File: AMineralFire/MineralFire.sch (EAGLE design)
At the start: 61 parts, among them IC1 LM358, Q1 20MHz, Q2 20MHz, T1 200mA/40V, U1 328P, U2 328P, U3 7805

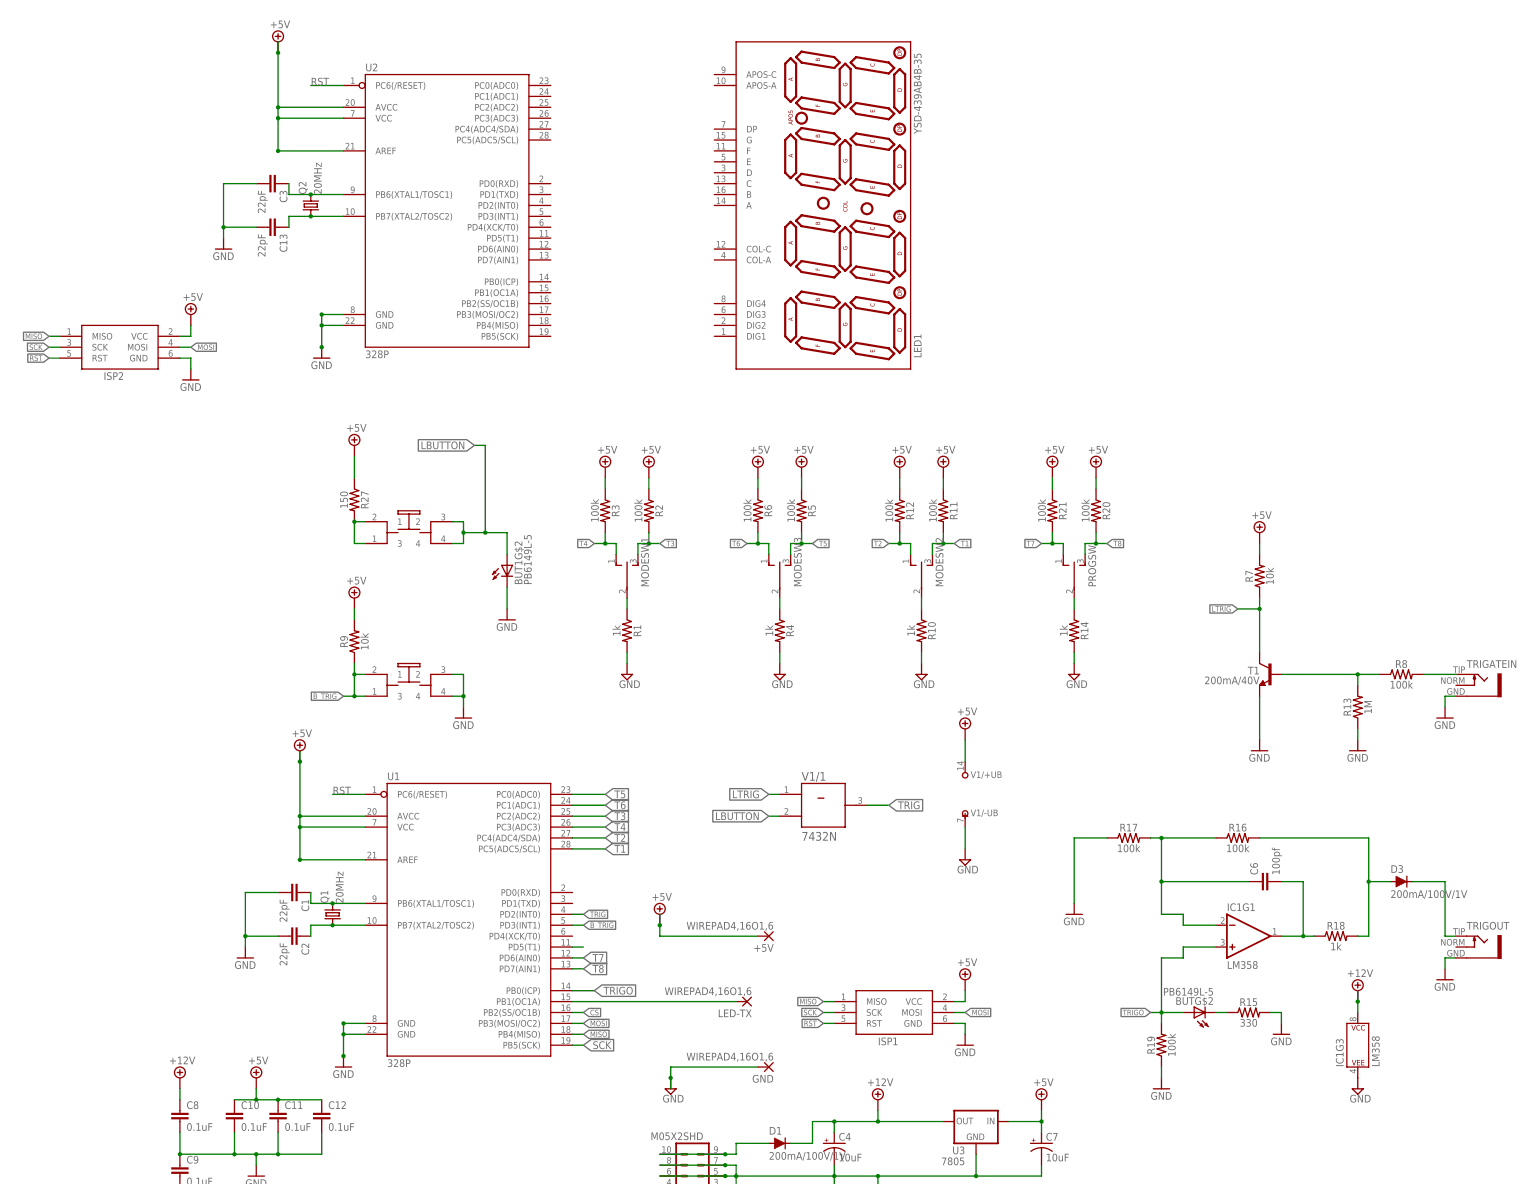
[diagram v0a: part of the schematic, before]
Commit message: adding Display
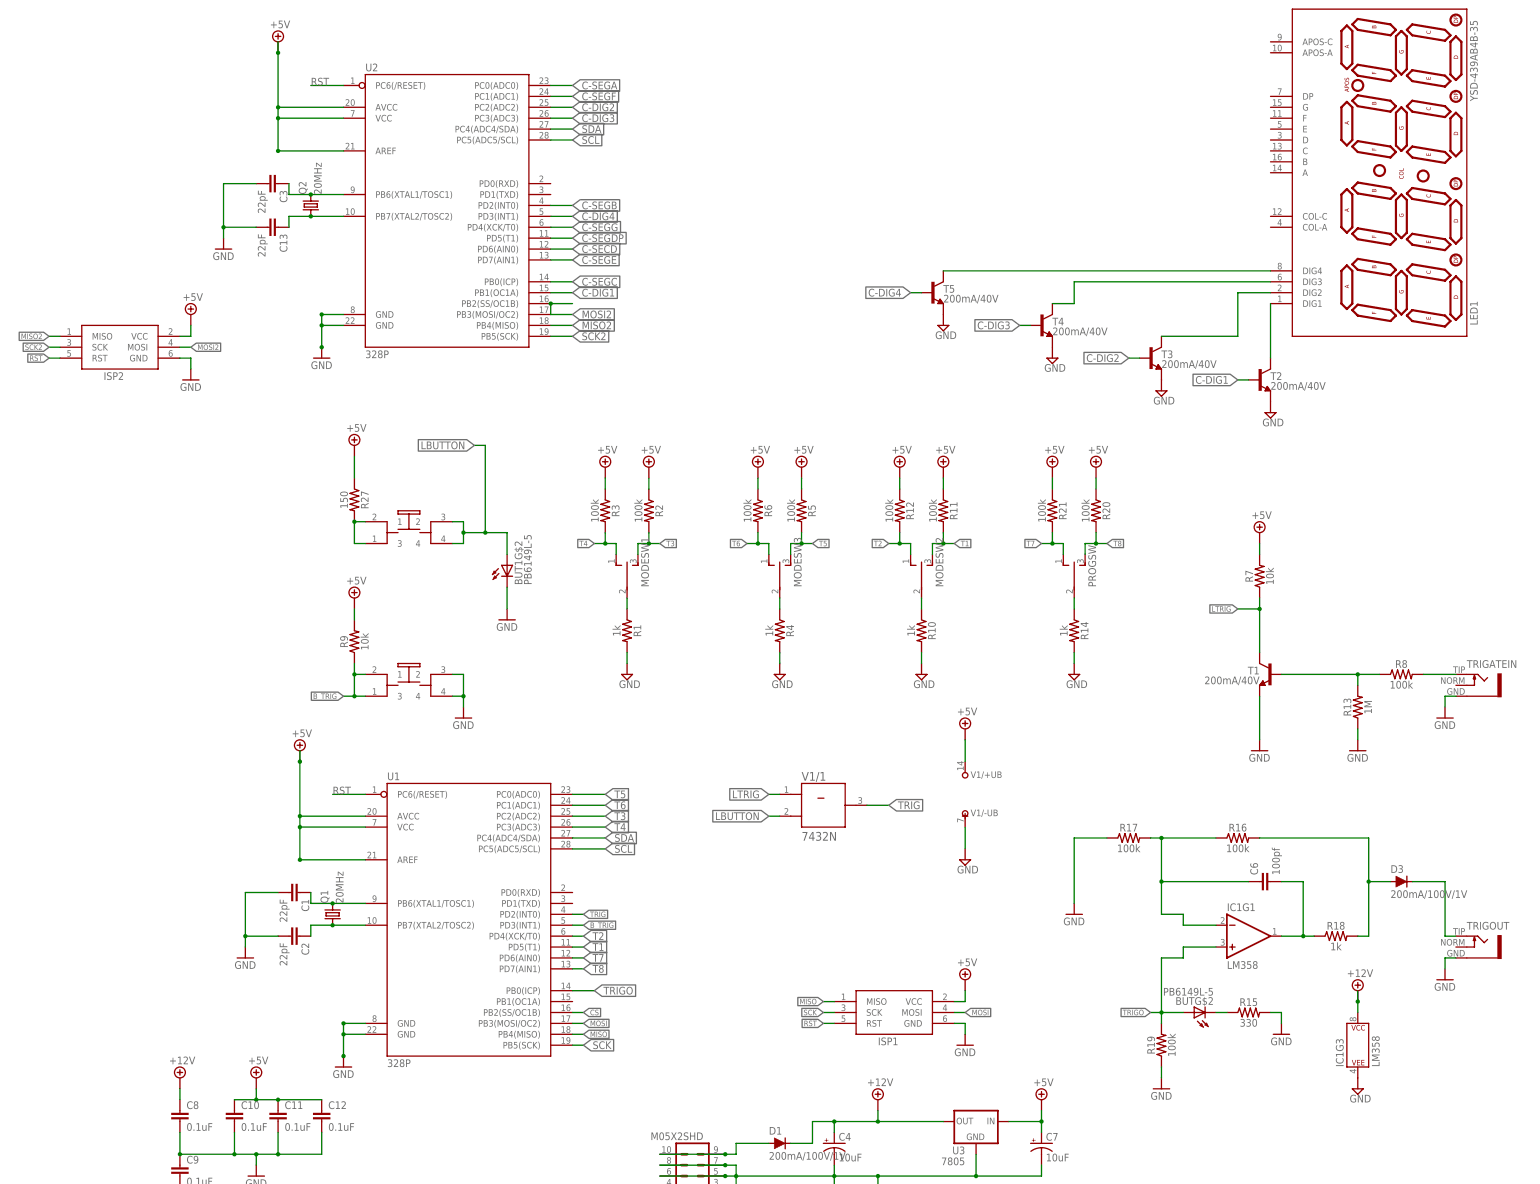
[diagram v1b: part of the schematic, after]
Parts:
- removed +5V, GND, LED-TX: WIREPAD4,16O1,6, wirepad:WIREPAD4,16O1,6
- added T2, T3, T4, T5: 200mA/40V, SparkFun-DiscreteSemi:TRANS_NPN-2N3904
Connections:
- removed net PR1: U1.PD5(T1)
- new net C-DIG1: T2.B, U2.PB1(OC1A)
- new net C-DIG2: T3.B, U2.PC2(ADC2)
- new net C-DIG3: T4.B, U2.PC3(ADC3)
- new net C-DIG4: T5.B, U2.PD3(INT1)
- new net C-SECD: U2.PD6(AIN0)
- new net C-SEGA: U2.PC0(ADC0)
- new net C-SEGB: U2.PD2(INT0)
- new net C-SEGC: U2.PB0(ICP)
- new net C-SEGDP: U2.PD5(T1)
- new net C-SEGE: U2.PD7(AIN1)
- new net C-SEGF: U2.PC1(ADC1)
- new net C-SEGG: U2.PD4(XCK/T0)
- new net MISO2: ISP2.MISO, U2.PB4(MISO)
- new net MOSI2: ISP2.MOSI, U2.PB2(SS/OC1B), U2.PB3(MOSI/OC2)
- new net N$13: LED1.DIG2, T3.C
- new net N$14: LED1.DIG3, T4.C
- new net N$16: LED1.DIG4, T5.C
- new net SCK2: ISP2.SCK, U2.PB5(SCK)
- new net SCL: U1.PC5(ADC5/SCL), U2.PC5(ADC5/SCL)
- new net SDA: U1.PC4(ADC4/SDA), U2.PC4(ADC4/SDA)
- net +5V: no longer +5V.P
- net GND: now also T2.E, T3.E, T4.E, T5.E; no longer GND.P
- net MISO: no longer ISP2.MISO
- net MOSI: no longer ISP2.MOSI
- net N$5: now also LED1.DIG1, T2.C; no longer LED-TX.P, U1.PB1(OC1A)
- net SCK: no longer ISP2.SCK
- net T1: now also U1.PD5(T1); no longer U1.PC5(ADC5/SCL)
- net T2: now also U1.PD4(XCK/T0); no longer U1.PC4(ADC4/SDA)
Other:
- moved on the sheet: LED1

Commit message: Vishray 7 segment display
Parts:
- removed LED1: YSD-439AB4B-35, SparkFun-LED:7-SEGMENT-4DIGIT-10MM-BLUE
- added DS1: TDCG1060M, TDCG1060M:TDCG1060M
- added Q3, Q4, Q5, Q6, Q7, Q8, Q9: 2N3906, transistor-pnp:2N3906
- added R22, R23, R24, R25, R26, R28, R29: 68OHM-0603-1/10W-1%, SparkFun-Resistors:68OHM-0603-1/10W-1%
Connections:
- removed net C-SECD: U2.PD6(AIN0)
- new net AN-A: DS1.ANODE_A, R29.1
- new net AN-B: DS1.ANODE_B, R24.1
- new net AN-C: DS1.ANODE_C, R28.1
- new net AN-D: DS1.ANODE_D, R23.1
- new net AN-E: DS1.ANODE_E, R22.1
- new net AN-F: DS1.ANODE_F, R26.1
- new net AN-G: DS1.ANODE_G, R25.1
- new net C-SEGD: Q3.B, U2.PD6(AIN0)
- new net D1: DS1.COMMON_CATHODE_D1, T2.C
- new net D2: DS1.COMMON_CATHODE_D2, T3.C
- new net D3: DS1.COMMON_CATHODE_D3, T4.C
- new net D4: DS1.COMMON_CATHODE_D4, T5.C
- new net N$17: Q6.C, R25.2
- new net N$19: BUT1G$2.C, R27.1
- new net N$20: Q5.C, R29.2
- net +5V: now also BUT1G$1.1, BUT1G$1.3, Q3.E, Q4.E, Q5.E, Q6.E, Q7.E, Q8.E, Q9.E; no longer R27.1
- net C-SEGA: now also Q5.B
- net C-SEGB: now also Q9.B
- net C-SEGC: now also Q7.B
- net C-SEGE: now also Q4.B
- net C-SEGF: now also Q8.B
- net C-SEGG: now also Q6.B
- net GND: now also R27.2; no longer BUT1G$2.C
- net LBUTTON: now also BUT1G$1.2, BUT1G$1.4, BUT1G$2.A; no longer BUT1G$1.1, BUT1G$1.3, R27.2
- net N$11: now also Q3.C, R23.2; no longer BUT1G$1.2, BUT1G$1.4, BUT1G$2.A
- net N$13: now also Q9.C, R24.2; no longer LED1.DIG2, T3.C
- net N$14: now also Q8.C, R26.2; no longer LED1.DIG3, T4.C
- net N$16: now also Q7.C, R28.2; no longer LED1.DIG4, T5.C
- net N$5: now also Q4.C, R22.2; no longer LED1.DIG1, T2.C
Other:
- moved on the sheet: BUT1G$2, R27, T2, T3, T4, T5

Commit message: moving to SMD
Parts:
- R22, R23: value 68OHM-0603-1/10W-1% -> 100; device SparkFun-Resistors:68OHM-0603-1/10W-1% -> SparkFun-Resistors:100OHM-0603-1/4W-5%
- R24, R25, R26, R28, R29: value 68OHM-0603-1/10W-1% -> 100; device SparkFun-Resistors:68OHM-0603-1/10W-1% -> SparkFun-Resistors:100OHM-HORIZ_KIT-1/4W-1%
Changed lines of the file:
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@@
 <grid distance="0.1" unitdist="inch" unit="inch" style="lines" multiple="1" display="no" altdistance="0.01" altunitdist="inch" altunit="inch"/>
 <layers>
-<layer number="1" name="Top" color="4" fill="1" visible="no" active="no"/>
-<layer number="2" name="Route2" color="1" fill="3" visible="no" active="no"/>
-<layer number="3" name="Route3" color="4" fill="3" visible="no" active="no"/>
-<layer number="4" name="Route4" color="1" fill="4" visible="no" active="no"/>
-<layer number="5" name="Route5" color="4" fill="4" visible="no" active="no"/>
-<layer number="6" name="Route6" color="1" fill="8" visible="no" active="no"/>
-<layer number="7" name="Route7" color="4" fill="8" visible="no" active="no"/>
-<layer number="8" name="Route8" color="1" fill="2" visible="no" active="no"/>
-<layer number="9" name="Route9" color="4" fill="2" visible="no" active="no"/>
-<layer number="10" name="Route10" color="1" fill="7" visible="no" active="no"/>
-<layer number="11" name="Route11" color="4" fill="7" visible="no" active="no"/>
-<layer number="12" name="Route12" color="1" fill="5" visible="no" active="no"/>
-<layer number="13" name="Route13" color="4" fill="5" visible="no" active="no"/>
-<layer number="14" name="Route14" color="1" fill="6" visible="no" active="no"/>
-<layer number="15" name="Route15" color="4" fill="6" visible="no" active="no"/>
-<layer number="16" name="Bottom" color="1" fill="1" visible="no" active="no"/>
-<layer number="17" name="Pads" color="2" fill="1" visible="no" active="no"/>
-<layer number="18" name="Vias" color="2" fill="1" visible="no" active="no"/>
-<layer number="19" name="Unrouted" color="6" fill="1" visible="no" active="no"/>
-<layer number="20" name="Dimension" color="15" fill="1" visible="no" active="no"/>
-<layer number="21" name="tPlace" color="7" fill="1" visible="no" active="no"/>
-<layer number="22" name="bPlace" color="7" fill="1" visible="no" active="no"/>
-<layer number="23" name="tOrigins" color="15" fill="1" visible="no" active="no"/>
-<layer number="24" name="bOrigins" color="15" fill="1" visible="no" active="no"/>
-<layer number="25" name="tNames" color="7" fill="1" visible="no" active="no"/>
-<layer number="26" name="bNames" color="7" fill="1" visible="no" active="no"/>
-<layer number="27" name="tValues" color="7" fill="1" visible="no" active="no"/>
-<layer number="28" name="bValues" color="7" fill="1" visible="no" active="no"/>
+<layer number="1" name="Top" color="4" fill="1" visible="yes" active="no"/>
+<layer number="2" name="Route2" color="1" fill="3" visible="yes" active="no"/>
+<layer number="3" name="Route3" color="4" fill="3" visible="yes" active="no"/>
+<layer number="4" name="Route4" color="1" fill="4" visible="yes" active="no"/>
+<layer number="5" name="Route5" color="4" fill="4" visible="yes" active="no"/>
+<layer number="6" name="Route6" color="1" fill="8" visible="yes" active="no"/>
+<layer number="7" name="Route7" color="4" fill="8" visible="yes" active="no"/>
+<layer number="8" name="Route8" color="1" fill="2" visible="yes" active="no"/>
+<layer number="9" name="Route9" color="4" fill="2" visible="yes" active="no"/>
+<layer number="10" name="Route10" color="1" fill="7" visible="yes" active="no"/>
+<layer number="11" name="Route11" color="4" fill="7" visible="yes" active="no"/>
+<layer number="12" name="Route12" color="1" fill="5" visible="yes" active="no"/>
+<layer number="13" name="Route13" color="4" fill="5" visible="yes" active="no"/>
+<layer number="14" name="Route14" color="1" fill="6" visible="yes" active="no"/>
+<layer number="15" name="Route15" color="4" fill="6" visible="yes" active="no"/>
+<layer number="16" name="Bottom" color="1" fill="1" visible="yes" active="no"/>
+<layer number="17" name="Pads" color="2" fill="1" visible="yes" active="no"/>
+<layer number="18" name="Vias" color="2" fill="1" visible="yes" active="no"/>
+<layer number="19" name="Unrouted" color="6" fill="1" visible="yes" active="no"/>
+<layer number="20" name="Dimension" color="15" fill="1" visible="yes" active="no"/>
+<layer number="21" name="tPlace" color="7" fill="1" visible="yes" active="no"/>
+<layer number="22" name="bPlace" color="7" fill="1" visible="yes" active="no"/>
+<layer number="23" name="tOrigins" color="15" fill="1" visible="yes" active="no"/>
+<layer number="24" name="bOrigins" color="15" fill="1" visible="yes" active="no"/>
+<layer number="25" name="tNames" color="7" fill="1" visible="yes" active="no"/>
+<layer number="26" name="bNames" color="7" fill="1" visible="yes" active="no"/>
+<layer number="27" name="tValues" color="7" fill="1" visible="yes" active="no"/>
+<layer number="28" name="bValues" color="7" fill="1" visible="yes" active="no"/>
 <layer number="29" name="tStop" color="7" fill="3" visible="no" active="no"/>
 <layer number="30" name="bStop" color="7" fill="6" visible="no" active="no"/>
@@
 <layer number="35" name="tGlue" color="7" fill="4" visible="no" active="no"/>
 <layer number="36" name="bGlue" color="7" fill="5" visible="no" active="no"/>
-<layer number="37" name="tTest" color="7" fill="1" visible="no" active="no"/>
-<layer number="38" name="bTest" color="7" fill="1" visible="no" active="no"/>
+<layer number="37" name="tTest" color="7" fill="1" visible="yes" active="no"/>
+<layer number="38" name="bTest" color="7" fill="1" visible="yes" active="no"/>
 <layer number="39" name="tKeepout" color="4" fill="11" visible="no" active="no"/>
 <layer number="40" name="bKeepout" color="1" fill="11" visible="no" active="no"/>
@@
 <layer number="44" name="Drills" color="7" fill="1" visible="no" active="no"/>
 <layer number="45" name="Holes" color="7" fill="1" visible="no" active="no"/>
-<layer number="46" name="Milling" color="3" fill="1" visible="no" active="no"/>
-<layer number="47" name="Measures" color="7" fill="1" visible="no" active="no"/>
-<layer number="48" name="Document" color="7" fill="1" visible="no" active="no"/>
-<layer number="49" name="Reference" color="7" fill="1" visible="no" active="no"/>
-<layer number="50" name="dxf" color="7" fill="1" visible="no" active="no"/>
-<layer number="51" name="tDocu" color="7" fill="1" visible="no" active="no"/>
-<layer number="52" name="bDocu" color="7" fill="1" visible="no" active="no"/>
-<layer number="53" name="tGND_GNDA" color="7" fill="9" visible="no" active="no"/>
-<layer number="54" name="bGND_GNDA" color="1" fill="9" visible="no" active="no"/>
-<layer number="56" name="wert" color="7" fill="1" visible="no" active="no"/>
-<layer number="57" name="tCAD" color="7" fill="1" visible="no" active="no"/>
-<layer number="59" name="tCarbon" color="7" fill="1" visible="no" active="no"/>
-<layer number="60" name="bCarbon" color="7" fill="1" visible="no" active="no"/>
+<layer number="46" name="Milling" color="3" fill="1" visible="yes" active="no"/>
+<layer number="47" name="Measures" color="7" fill="1" visible="yes" active="no"/>
+<layer number="48" name="Document" color="7" fill="1" visible="yes" active="no"/>
+<layer number="49" name="Reference" color="7" fill="1" visible="yes" active="no"/>
+<layer number="50" name="dxf" color="7" fill="1" visible="yes" active="no"/>
+<layer number="51" name="tDocu" color="7" fill="1" visible="yes" active="no"/>
+<layer number="52" name="bDocu" color="7" fill="1" visible="yes" active="no"/>
+<layer number="53" name="tGND_GNDA" color="7" fill="9" visible="yes" active="no"/>
+<layer number="54" name="bGND_GNDA" color="1" fill="9" visible="yes" active="no"/>
+<layer number="56" name="wert" color="7" fill="1" visible="yes" active="no"/>
+<layer number="57" name="tCAD" color="7" fill="1" visible="yes" active="no"/>
+<layer number="59" name="tCarbon" color="7" fill="1" visible="yes" active="no"/>
+<layer number="60" name="bCarbon" color="7" fill="1" visible="yes" active="no"/>
 <layer number="90" name="Modules" color="5" fill="1" visible="yes" active="yes"/>
 <layer number="91" name="Nets" color="2" fill="1" visible="yes" active="yes"/>
@@
 <part name="SUPPLY39" library="supply2" deviceset="+5V" device=""/>
 <part name="SUPPLY40" library="supply2" deviceset="+5V" device=""/>
-<part name="R22" library="SparkFun-Resistors" deviceset="68OHM" device="-0603-1/10W-1%"/>
-<part name="R23" library="SparkFun-Resistors" deviceset="68OHM" device="-0603-1/10W-1%"/>
-<part name="R24" library="SparkFun-Resistors" deviceset="68OHM" device="-0603-1/10W-1%"/>
-<part name="R25" library="SparkFun-Resistors" deviceset="68OHM" device="-0603-1/10W-1%"/>
-<part name="R26" library="SparkFun-Resistors" deviceset="68OHM" device="-0603-1/10W-1%"/>
-<part name="R28" library="SparkFun-Resistors" deviceset="68OHM" device="-0603-1/10W-1%"/>
-<part name="R29" library="SparkFun-Resistors" deviceset="68OHM" device="-0603-1/10W-1%"/>
+<part name="R22" library="SparkFun-Resistors" deviceset="100OHM" device="-0603-1/4W-5%" value="100"/>
+<part name="R23" library="SparkFun-Resistors" deviceset="100OHM" device="-0603-1/4W-5%" value="100"/>
+<part name="R24" library="SparkFun-Resistors" deviceset="100OHM" device="-HORIZ_KIT-1/4W-1%" value="100"/>
+<part name="R25" library="SparkFun-Resistors" deviceset="100OHM" device="-HORIZ_KIT-1/4W-1%" value="100"/>
+<part name="R26" library="SparkFun-Resistors" deviceset="100OHM" device="-HORIZ_KIT-1/4W-1%" value="100"/>
+<part name="R28" library="SparkFun-Resistors" deviceset="100OHM" device="-HORIZ_KIT-1/4W-1%" value="100"/>
+<part name="R29" library="SparkFun-Resistors" deviceset="100OHM" device="-HORIZ_KIT-1/4W-1%" value="100"/>
 </parts>
 <sheets>

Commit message: Continuing move to SMD
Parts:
- added IC2: OP-AMP, SparkFun-IC-Amplifiers:OPAMP-DUALU
- C1, C13, C2, C3: device SparkFun-Capacitors:22PF-PTH-2.54MM-200V-5% -> SparkFun-Capacitors:22PF-0603-50V-5%
- C10, C11, C12, C8, C9: device SparkFun-Capacitors:0.1UF-KIT-EZ-50V-20% -> SparkFun-Capacitors:0.1UF-0603-25V-5%
- C4, C5, C7: value 10uF -> 10µF; device SparkFun-Capacitors:10UF-POLAR-RADIAL-2.5MM-25V-20% -> SparkFun-Capacitors:10UF-POLAR-EIA6032-25V-10%
- D3: value 200mA/100V/1V -> 250mA/100V; device SparkFun-DiscreteSemi:DIODE-1N4148 -> SparkFun-DiscreteSemi:DIODE-BAS16J
- Q1, Q2: device adafruit:CRYSTALHC49U70 -> adafruit:CRYSTALHC49UP
- R1, R10, R14, R18, R4: device SparkFun-Resistors:1KOHM-HORIZ-1/4W-5% -> SparkFun-Resistors:1KOHM-0603-1/10W-1%
- R11, R12, R16, R17, R19, R2, R20, R21, R3, R8: device SparkFun-Resistors:100KOHM-HORIZ-1/4W-5% -> SparkFun-Resistors:100KOHM-0603-1/10W-1%
- R13: device SparkFun-Resistors:1MOHM-HORIZ-1/4W-5% -> SparkFun-Resistors:1MOHM-0603-1/4W-5%
- R15: device SparkFun-Resistors:330OHM-HORIZ-1/10W-5% -> SparkFun-Resistors:330OHM-0603-1/10W-1%
- R22, R23: value 100 -> 68OHM-0603-1/10W-1%; device SparkFun-Resistors:100OHM-0603-1/4W-5% -> SparkFun-Resistors:68OHM-0603-1/10W-1%
- R24, R25, R26, R28, R29: value 100 -> 68OHM-0603-1/10W-1%; device SparkFun-Resistors:100OHM-HORIZ_KIT-1/4W-1% -> SparkFun-Resistors:68OHM-0603-1/10W-1%
- R27: value 150 -> 100k; device SparkFun-Resistors:100KOHM-HORIZ-1/4W-5% -> SparkFun-Resistors:100KOHM-0603-1/10W-1%
- R6: value 100k -> 100K; device SparkFun-Resistors:100KOHM-HORIZ-1/4W-5% -> SparkFun-Resistors:100KOHM-0402-1/16W-1%
- R7: device SparkFun-Resistors:10KOHM-HORIZ-1/4W-5% -> SparkFun-Resistors:10KOHM-0603-1/10W-1%
- U3: value 7805 -> +12v; device SparkFun-IC-Power:V_REG_78XX-TO-220 -> SparkFun-IC-Power:V_REG_78XX7812
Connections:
- net N$32: now also IC2G1.-IN; no longer IC1G1.-IN
- net N$33: now also IC2G1.OUT; no longer IC1G1.OUT
- net TRIGO: now also IC2G1.+IN; no longer IC1G1.+IN
